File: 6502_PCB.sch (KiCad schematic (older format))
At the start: 19 parts

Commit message: Continued Editing Schematic
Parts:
- removed SW? (x3): SW_Push, symbol Switch:SW_Push
- added R? (x5): 1k, symbol Device:R
- added SW? (x4): SW_Push, symbol Switch:SW_Push
- RV?: value R_POT -> 10k
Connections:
- net +5V: now also IC?.20 (VDD), IC?.27 (~WE), IC?.28 (VCC), U?.14 (VCC), U?.15 (A/VEE), U?.2 (VDD), R?.2, R?.2, R?.2, R?.2, R?.2
- net GND: now also IC?.1 (VSS), IC?.14 (VSS), IC?.22 (~OE), RV?.1, SW?.2, U?.16 (K), U?.7 (GND), X?.4 (GND), SW?.2, SW?.2, SW?.2, SW?.2
- net at U?.10 (3B): now also IC?.20 (~CE), U?.5 (2B), U?.8 (3Y)
- net at U?.11 (4Y): now also IC?.20 (CE#)
- net A15: now reaches U?.12 (4A)
- net A15: now also IC?.25 (A15), U?.13 (4B)
- net A14: now reaches U?.4 (2A)
- net A14: now also IC?.1 (A14), IC?.1 (A14), IC?.22 (OE#), IC?.24 (A14)
- net at U?.6 (2Y): now also IC?.23 (CS2B)
- net at U?.9 (3A): now also IC?.22 (RWB), IC?.27 (WE#), IC?.34 (RWB)
- net PB0: now reaches IC?.10 (PB0)
- net PB0: now also U?.7 (DB0)
- net PB1: now reaches IC?.11 (PB1)
- net PB1: now also U?.8 (DB1)
- net PB2: now reaches IC?.12 (PB2)
- net PB2: now also U?.9 (DB2)
- net PB3: now reaches IC?.13 (PB3)
- net PB3: now also U?.10 (DB3)
- net PB4: now reaches IC?.14 (PB4)
- net PB4: now also U?.11 (DB4)
- net PB5: now reaches IC?.15 (PB5)
- net PB5: now also U?.12 (DB5)
- net PB6: now reaches IC?.16 (PB6)
- net PB6: now also U?.13 (DB6)
- net PB7: now reaches IC?.17 (PB7)
- net PB7: now also U?.14 (DB7)
- net at IC?.2 (PA0): now also SW?.1, R?.1
- net at IC?.21 (IRQB): now also IC?.2 (RDY), IC?.34 (RESB), IC?.4 (IRQB), R?.2
- net A13: now reaches IC?.24 (CS1)
- net A13: now also IC?.23 (A13), IC?.26 (A13), IC?.26 (A13)
- net at IC?.25 (PHI2): now also IC?.37 (PHI2), X?.5 (OUT)
- net at IC?.3 (PA1): now also R?.1, SW?.1
- net A3: now reaches IC?.35 (RS3)
- net A3: now also IC?.12 (A3), IC?.7 (A3), IC?.7 (A3)
- net A2: now reaches IC?.36 (RS2)
- net A2: now also IC?.11 (A2), IC?.8 (A2), IC?.8 (A2)
- net A1: now reaches IC?.37 (RS1)
- net A1: now also IC?.10 (A1), IC?.9 (A1), IC?.9 (A1)
- net A0: now reaches IC?.38 (RS0)
- net A0: now also IC?.10 (A0), IC?.10 (A0), IC?.9 (A0)
- net at IC?.4 (PA2): now also R?.1, SW?.1
- net at IC?.5 (PA3): now also R?.1, SW?.1
- net at IC?.6 (PA4): now also R?.1, SW?.1
- net at IC?.7 (PA5): now also U?.4 (RS)
- net at IC?.8 (PA6): now also U?.5 (R/W)
- net at IC?.9 (PA7): now also U?.6 (E)
- net A4: now reaches IC?.13 (A4)
- net A4: now also IC?.6 (A4), IC?.6 (A4)
- net A5: now reaches IC?.14 (A5)
- net A5: now also IC?.5 (A5), IC?.5 (A5)
- net A6: now reaches IC?.15 (A6)
- net A6: now also IC?.4 (A6), IC?.4 (A6)
- net A7: now reaches IC?.16 (A7)
- net A7: now also IC?.3 (A7), IC?.3 (A7)
- net A8: now reaches IC?.17 (A8)
- net A8: now also IC?.25 (A8), IC?.25 (A8)
- net A9: now reaches IC?.18 (A9)
- net A9: now also IC?.24 (A9), IC?.24 (A9)
- net A10: now reaches IC?.19 (A10)
- net A10: now also IC?.21 (A10), IC?.21 (A10)
- net A11: now reaches IC?.20 (A11)
- net A11: now also IC?.23 (A11), IC?.23 (A11)
- net A12: now reaches IC?.22 (A12)
- net A12: now also IC?.2 (A12), IC?.2 (A12)
- net at RV?.2: now also U?.3 (VO)
- no-connect marks 6 -> 14
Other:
- moved on the sheet: C?, IC?, RV?, SW?, U?

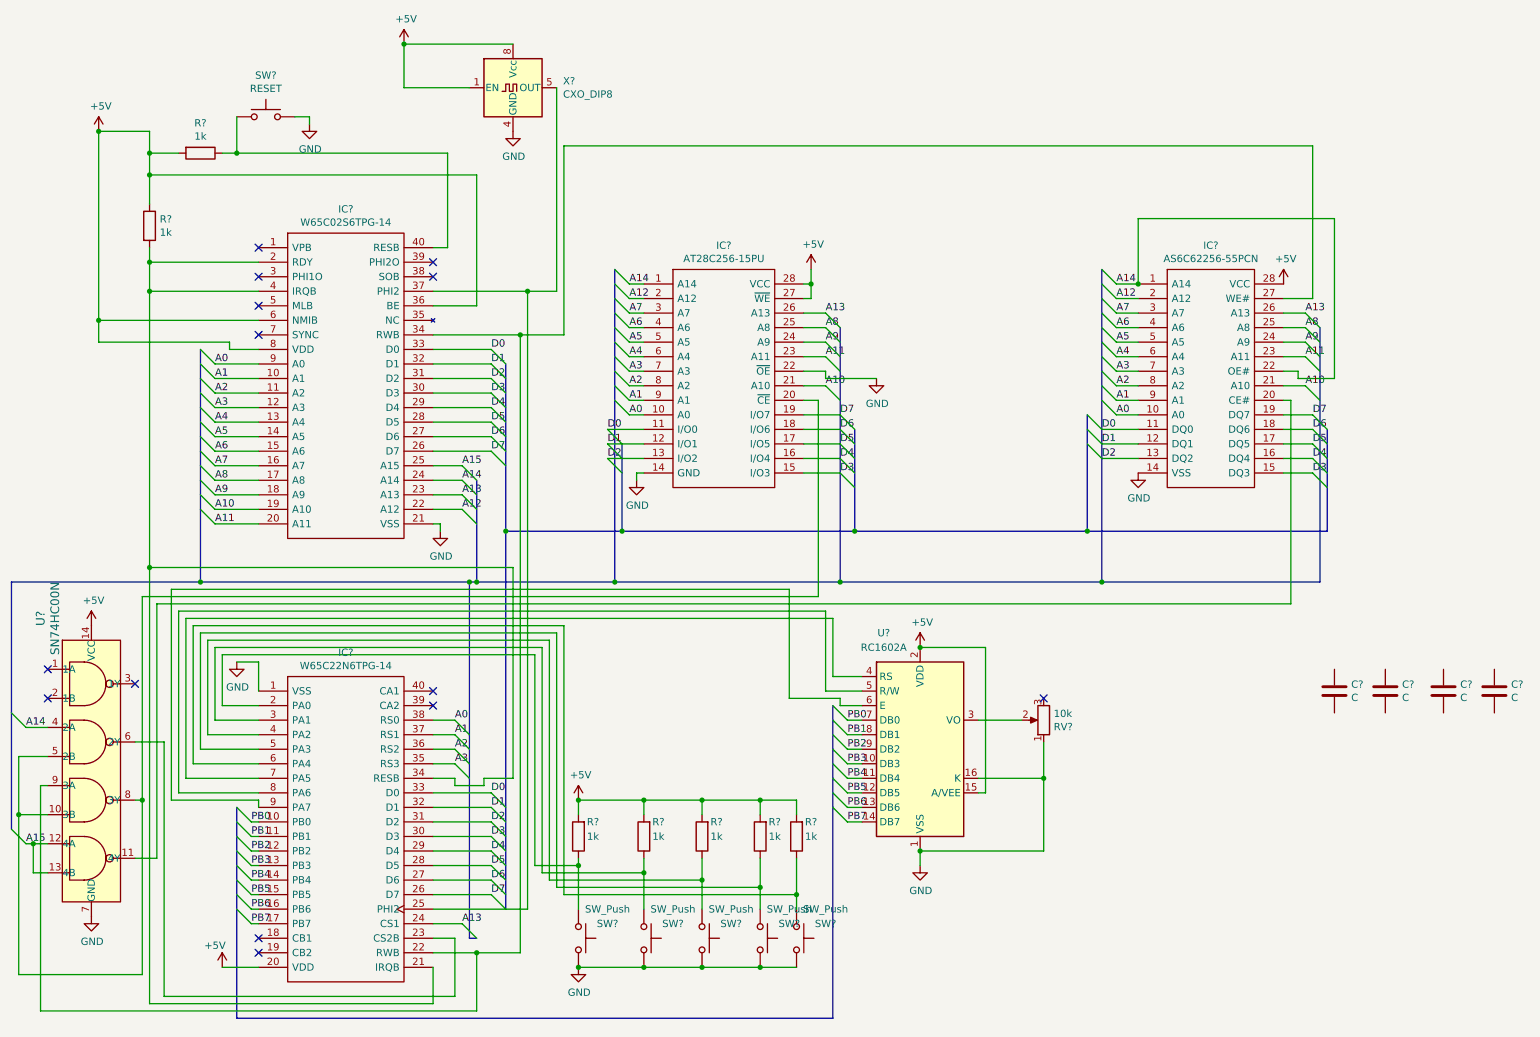
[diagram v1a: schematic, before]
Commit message: Corrected the wiring on the schematic
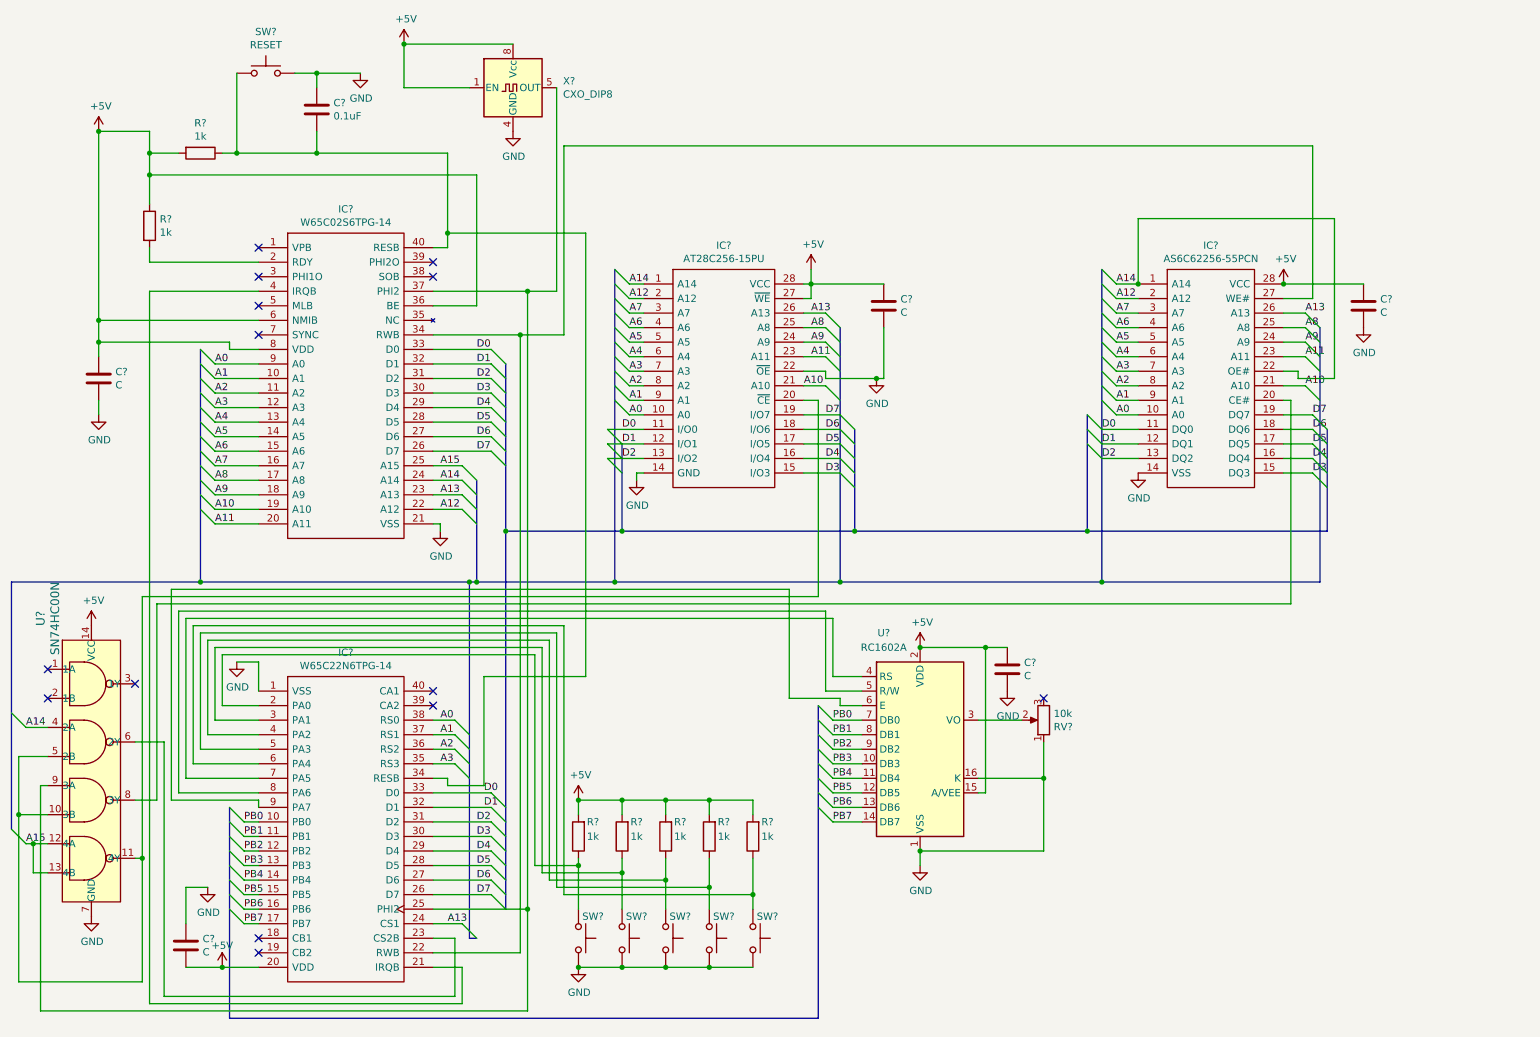
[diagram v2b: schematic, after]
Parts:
- added C?: C, symbol Device:C
- added C?: 0.1uF, symbol Device:C
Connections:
- net +5V: now also C?.1, C?.1, C?.1, C?.2, C?.1
- net GND: now also C?.1, C?.2, C?.2, C?.2, C?.1, C?.2
- net at IC?.20 (~CE), U?.10 (3B), U?.5 (2B): now also U?.11 (4Y); no longer U?.8 (3Y)
- net at IC?.20 (CE#): now also U?.8 (3Y); no longer U?.11 (4Y)
- net at IC?.22 (RWB), IC?.27 (WE#), IC?.34 (RWB): no longer U?.9 (3A)
- net at IC?.25 (PHI2), IC?.37 (PHI2), X?.5 (OUT): now also U?.9 (3A)
- net at IC?.40 (RESB), R?.1, SW?.1: now also IC?.34 (RESB), C?.2
- new net: IC?.21 (IRQB), IC?.4 (IRQB)
- new net: IC?.2 (RDY), R?.2
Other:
- moved on the sheet: C?, R?, SW?

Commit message: Associated Footprints and Started PCB Layout
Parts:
- C1, C2, C4, C5, C6: renamed from C?; value C -> 0.1uF; footprint (none) -> Capacitor_SMD:C_0805_2012Metric
- C3: renamed from C?; footprint (none) -> Capacitor_SMD:C_0805_2012Metric
- IC1, IC2: renamed from IC?; footprint DIP1524W56P254L5207H508Q40N -> Package_DIP:DIP-40_W15.24mm
- IC3: renamed from IC?; footprint DIP1556W56P254L3702H483Q28N -> Package_DIP:DIP-28_W15.24mm
- IC4: renamed from IC?; footprint DIP1587W140P254L3632H381Q28N -> Package_DIP:DIP-28_W15.24mm
- R1, R2, R3, R4, R5, R6, R7: renamed from R?; footprint (none) -> Resistor_SMD:R_0805_2012Metric
- RV1: renamed from RV?; footprint (none) -> digikey:TRIM_P090S-04F20BR10K
- SW1, SW2, SW3, SW4, SW5, SW6: renamed from SW?; footprint (none) -> Button_Switch_THT:SW_PUSH_6mm_H5mm
- U1: renamed from U?; footprint digikey-footprints:DIP-14_W3mm -> digikey:DIP-14_W3mm
- gave numbers to parts that had none: 2
